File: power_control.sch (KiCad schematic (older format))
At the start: 64 parts, among them J26 Conn_01x02, J27 Conn_01x02, J28 Conn_01x02, J29 Conn_01x02, J30 Conn_01x02, J31 Conn_01x02, J32 Conn_01x02, J33 Conn_01x02, U10 DRV8801PWP, U11 DRV8801PWP, U12 DRV8801PWP, U5 DRV8801PWP, U6 DRV8801PWP, U7 DRV8801PWP, U8 DRV8801PWP, U9 DRV8801PWP

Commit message: Final touches
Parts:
- removed C13, C16, C22, C25, C28, C34: 100nF, lsts-passives:C_0603, symbol Device:C
- removed C21, C33: 100uF, Capacitor_THT:CP_Radial_D5.0mm_P2.00mm, symbol Device:CP
- removed J28, J31: Conn_01x02, Connector_Molex:Molex_Micro-Fit_3.0_43045-0212_2x01_P3.00mm_Vertical, symbol Connector_Generic:Conn_01x02
- removed R34, R35, R40, R41: 10kR, lsts-passives:R_0603, symbol Device:R
- removed U10, U7: DRV8801PWP, Package_SO:HTSSOP-16-1EP_4.4x5mm_P0.65mm_EP3.4x5mm_Mask3x3mm_ThermalVias, symbol Driver_Motor:DRV8801PWP
- C10: renamed from C19; symbol Device:CP -> power_board-rescue:CP-Device
- C11: renamed from C20; footprint lsts-passives:C_0603 -> lsts_passives:C_0603
- C12: renamed from C23; footprint lsts-passives:C_0603 -> lsts_passives:C_0603
- C13: renamed from C24; footprint lsts-passives:C_0603 -> lsts_passives:C_0603
- C14: renamed from C26; footprint lsts-passives:C_0603 -> lsts_passives:C_0603
- C15: renamed from C27; footprint lsts-passives:C_0603 -> lsts_passives:C_0603
- C16: renamed from C29; symbol Device:CP -> power_board-rescue:CP-Device
- C17: renamed from C30; footprint lsts-passives:C_0603 -> lsts_passives:C_0603
- C18: renamed from C31; symbol Device:CP -> power_board-rescue:CP-Device
- C19: renamed from C32; footprint lsts-passives:C_0603 -> lsts_passives:C_0603
- C20: renamed from C35; footprint lsts-passives:C_0603 -> lsts_passives:C_0603
- C21: renamed from C36; footprint lsts-passives:C_0603 -> lsts_passives:C_0603
- C22: renamed from C37; footprint lsts-passives:C_0603 -> lsts_passives:C_0603
- C23: renamed from C38; footprint lsts-passives:C_0603 -> lsts_passives:C_0603
- C24: renamed from C39; symbol Device:CP -> power_board-rescue:CP-Device
- C25: renamed from C40; footprint lsts-passives:C_0603 -> lsts_passives:C_0603
- C26: renamed from C41; symbol Device:CP -> power_board-rescue:CP-Device
- C27: renamed from C42; footprint lsts-passives:C_0603 -> lsts_passives:C_0603
- C4: renamed from C11; footprint lsts-passives:C_0603 -> lsts_passives:C_0603
- C5: renamed from C12; footprint lsts-passives:C_0603 -> lsts_passives:C_0603
- C6: renamed from C14; footprint lsts-passives:C_0603 -> lsts_passives:C_0603
- C7: renamed from C15; footprint lsts-passives:C_0603 -> lsts_passives:C_0603
- C8: renamed from C17; symbol Device:CP -> power_board-rescue:CP-Device
- C9: renamed from C18; footprint lsts-passives:C_0603 -> lsts_passives:C_0603
- R30, R31, R32, R33: footprint lsts-passives:R_0603 -> lsts_passives:R_0603
- R34: renamed from R36; footprint lsts-passives:R_0603 -> lsts_passives:R_0603
- R35: renamed from R37; footprint lsts-passives:R_0603 -> lsts_passives:R_0603
- R36: renamed from R38; footprint lsts-passives:R_0603 -> lsts_passives:R_0603
- R37: renamed from R39; footprint lsts-passives:R_0603 -> lsts_passives:R_0603
- R38: renamed from R42; footprint lsts-passives:R_0603 -> lsts_passives:R_0603
- R39: renamed from R43; footprint lsts-passives:R_0603 -> lsts_passives:R_0603
- R40: renamed from R44; footprint lsts-passives:R_0603 -> lsts_passives:R_0603
- R41: renamed from R45; footprint lsts-passives:R_0603 -> lsts_passives:R_0603
- renumbered J26 to J25, J27 to J26, J29 to J27, J30 to J28, J32 to J29, J33 to J30, U5 to U3, U6 to U4, U8 to U5, U9 to U6, U11 to U7, U12 to U8
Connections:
- net labels removed: MTR7_EN, MTR7_PH, MTR7_SL, MTR8_EN, MTR8_PH, MTR8_SL
- wire segments 224 -> 168
- no-connect marks 16 -> 12

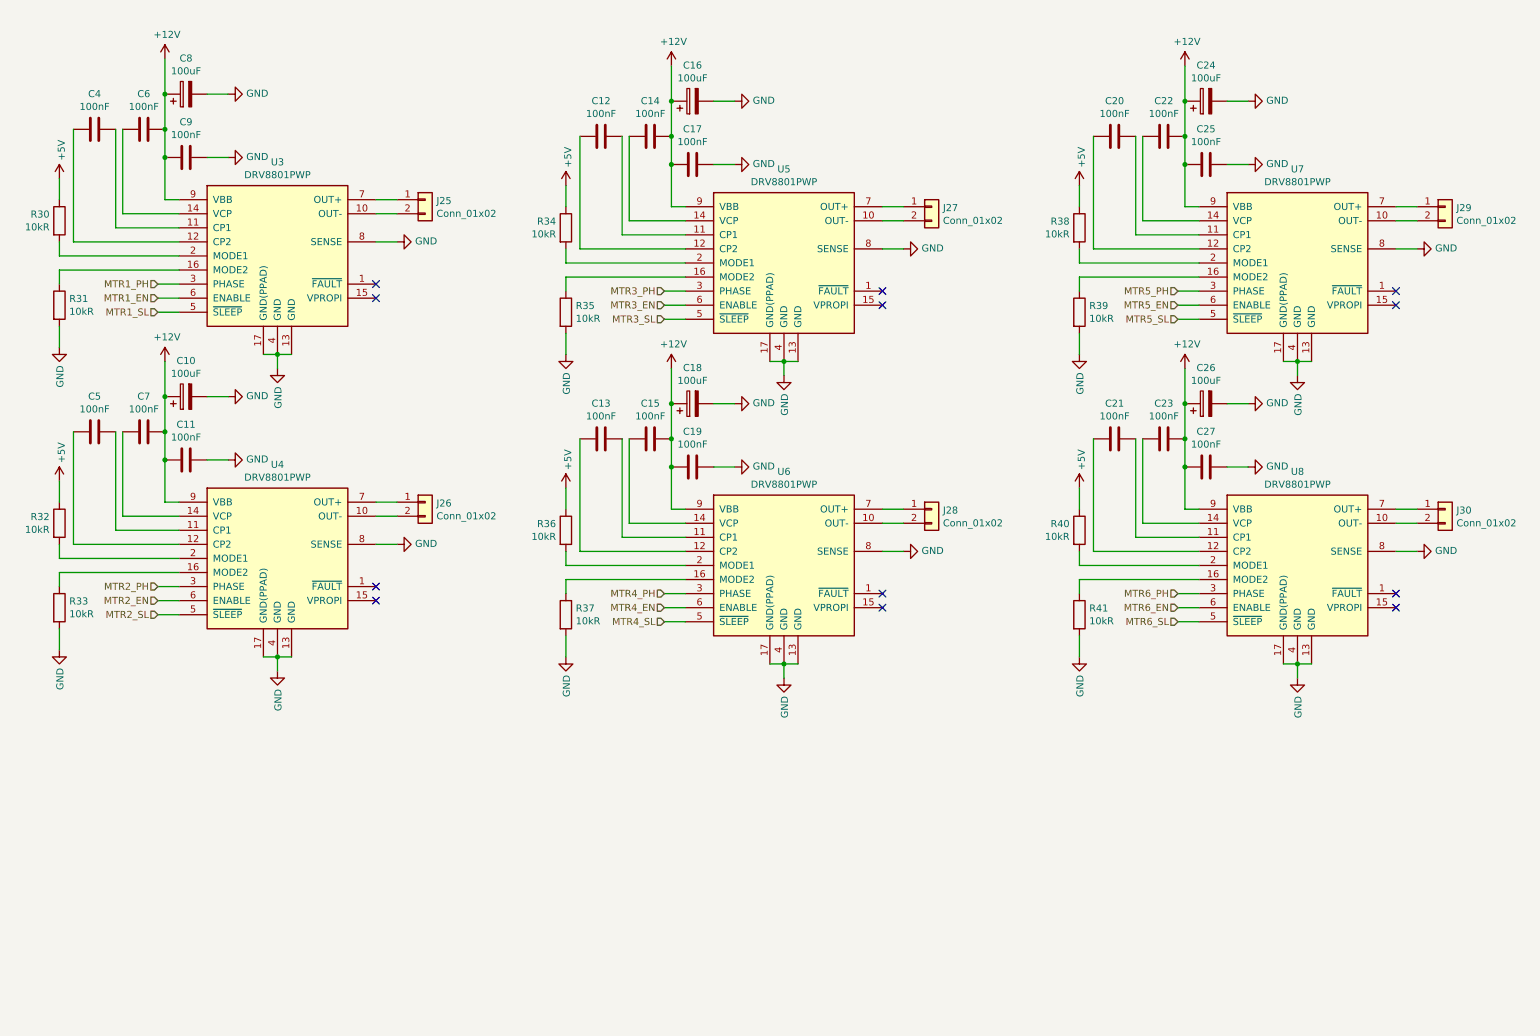
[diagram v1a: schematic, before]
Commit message: Replaced motor drivers
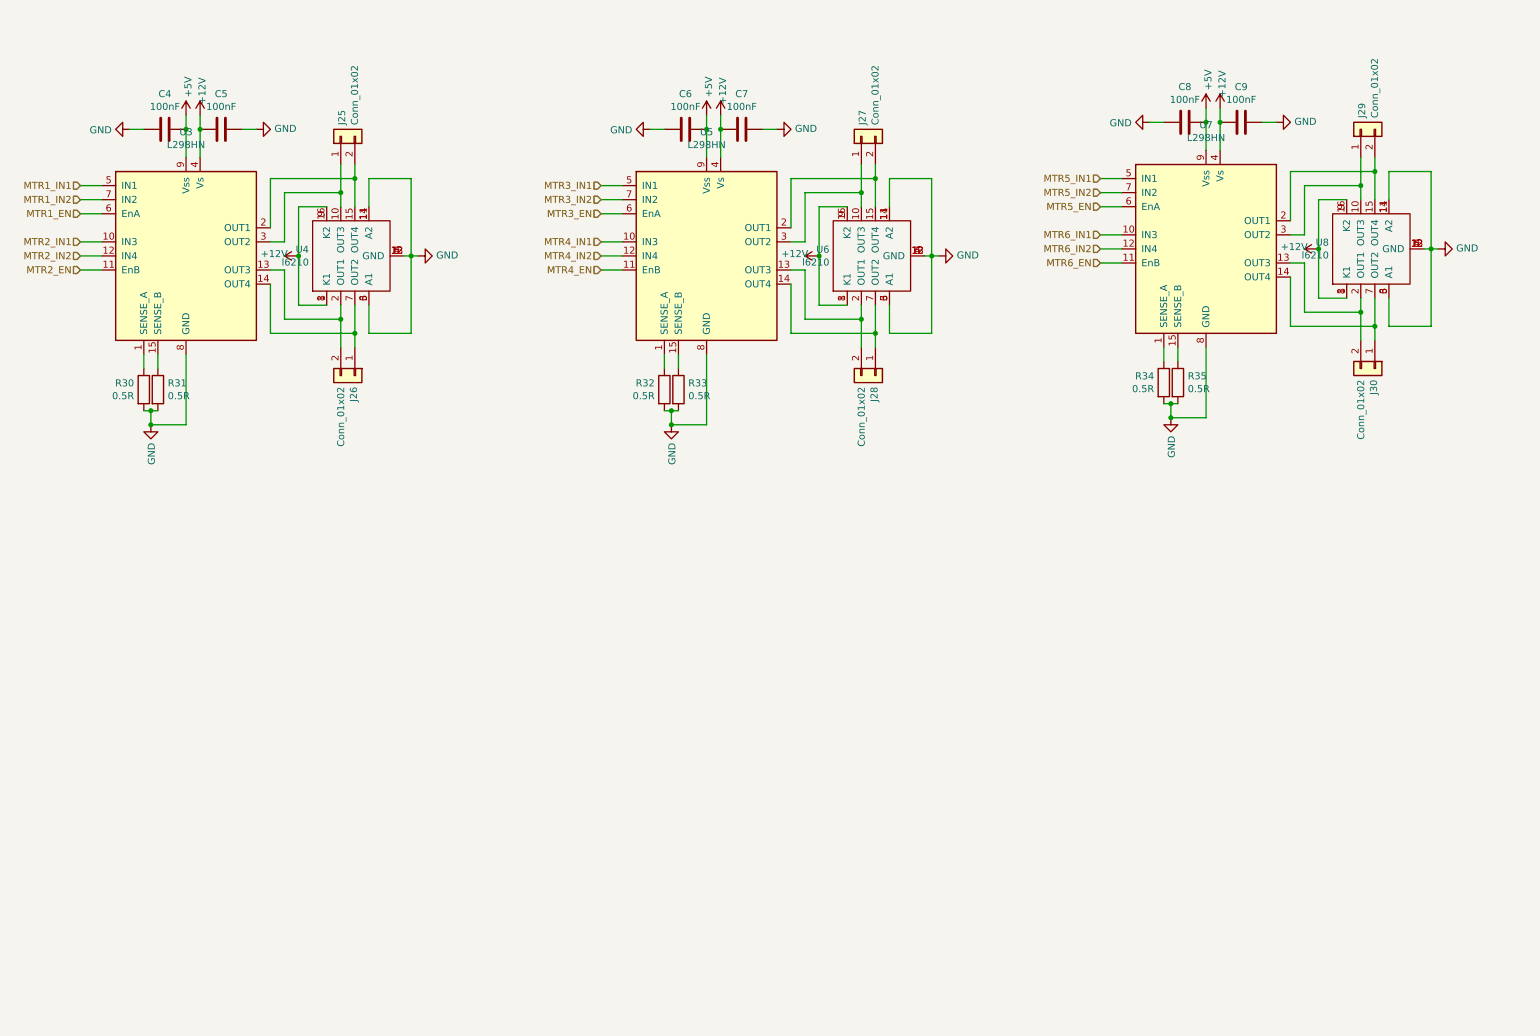
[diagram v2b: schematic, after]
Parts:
- removed C10, C16, C18, C24, C26, C8: 100uF, Capacitor_THT:CP_Radial_D5.0mm_P2.00mm, symbol power_board-rescue:CP-Device
- removed C11, C12, C13, C14, C15, C17, C19, C20, C21, C22, C23, C25, C27, C5: 100nF, lsts_passives:C_0603, symbol Device:C
- removed R30, R36, R37, R38, R39, R40, R41: 10kR, lsts_passives:R_0603, symbol Device:R
- removed U3, U4, U5, U6, U7, U8: DRV8801PWP, Package_SO:HTSSOP-16-1EP_4.4x5mm_P0.65mm_EP3.4x5mm_Mask3x3mm_ThermalVias, symbol Driver_Motor:DRV8801PWP
- added C6, C8: 100nF, lsts_passives:C_0603, symbol Device:C
- added R31: 0.5R, lsts_passives:R_0603, symbol Device:R
- added U3, U5, U7: L298HN, Package_TO_SOT_THT:TO-220-15_P2.54x2.54mm_StaggerOdd_Lead4.58mm_Vertical, symbol Driver_Motor:L298HN
- added U4, U6, U8: l6210, Package_DIP:DIP-16_W7.62mm, symbol Diode_Bridge:l6210
- R30: renamed from R31; value 10kR -> 0.5R
- R32, R33, R34, R35: value 10kR -> 0.5R
- renumbered C6 to C5
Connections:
- net +12V: now also C5.2, C7.2, U3.4 (Vs), U4.1 (K1), U4.16 (K2), U4.8 (K1), U4.9 (K2), U5.4 (Vs), U6.1 (K1), U6.16 (K2), U6.8 (K1), U6.9 (K2), U7.4 (Vs), U8.1 (K1), U8.16 (K2), U8.8 (K1), U8.9 (K2); no longer C5.1, C7.1
- net +5V: now also C4.1, C6.1, C8.1, U3.9 (Vss), U5.9 (Vss), U7.9 (Vss); no longer R32.1, R34.1
- net GND: now also C4.2, C5.1, C7.1, R32.2, R34.2, C6.2, C8.2, R31.2, U3.8 (GND), U4.11 (A2), U4.12 (GND), U4.13 (GND), U4.14 (A2), U4.3 (A1), U4.4 (GND), U4.5 (GND), U4.6 (A1), U5.8 (GND), U6.11 (A2), U6.12 (GND), U6.13 (GND), U6.14 (A2), U6.3 (A1), U6.4 (GND), U6.5 (GND), U6.6 (A1), U7.8 (GND), U8.11 (A2), U8.12 (GND), U8.13 (GND), U8.14 (A2), U8.3 (A1), U8.4 (GND), U8.5 (GND), U8.6 (A1)
- net MTR1_EN: now also U3.6 (EnA)
- net MTR2_EN: now also U3.11 (EnB)
- net MTR3_EN: now also U5.6 (EnA)
- net MTR4_EN: now also U5.11 (EnB)
- net MTR5_EN: now also U7.6 (EnA)
- net MTR6_EN: now also U7.11 (EnB)
- net at J25.1 (Pin_1): now also U3.3 (OUT2), U4.10 (OUT3)
- net at J25.2 (Pin_2): now also U3.2 (OUT1), U4.15 (OUT4)
- net at R30.1: now also U3.1 (SENSE_A)
- net at J26.2 (Pin_2): now also U3.13 (OUT3), U4.2 (OUT1)
- net at R33.1: now also U5.15 (SENSE_B)
- net at J26.1 (Pin_1): now also U3.14 (OUT4), U4.7 (OUT2)
- net at J27.2 (Pin_2): now also U5.2 (OUT1), U6.15 (OUT4)
- net at R35.1: now also U7.15 (SENSE_B)
- net at J27.1 (Pin_1): now also U5.3 (OUT2), U6.10 (OUT3)
- net at J28.2 (Pin_2): now also U5.13 (OUT3), U6.2 (OUT1)
- net at J28.1 (Pin_1): now also U5.14 (OUT4), U6.7 (OUT2)
- net at J29.2 (Pin_2): now also U7.2 (OUT1), U8.15 (OUT4)
- net at J29.1 (Pin_1): now also U7.3 (OUT2), U8.10 (OUT3)
- net at J30.2 (Pin_2): now also U7.13 (OUT3), U8.2 (OUT1)
- net at J30.1 (Pin_1): now also U7.14 (OUT4), U8.7 (OUT2)
- new net: R31.1, U3.15 (SENSE_B)
- new net: R32.1, U5.1 (SENSE_A)
- new net: R34.1, U7.1 (SENSE_A)
- new net MTR1_IN1: U3.5 (IN1)
- new net MTR1_IN2: U3.7 (IN2)
- new net MTR2_IN1: U3.10 (IN3)
- new net MTR2_IN2: U3.12 (IN4)
- new net MTR3_IN1: U5.5 (IN1)
- new net MTR3_IN2: U5.7 (IN2)
- new net MTR4_IN1: U5.10 (IN3)
- new net MTR4_IN2: U5.12 (IN4)
- new net MTR5_IN1: U7.5 (IN1)
- new net MTR5_IN2: U7.7 (IN2)
- new net MTR6_IN1: U7.10 (IN3)
- new net MTR6_IN2: U7.12 (IN4)
- no-connect marks 12 -> 0
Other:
- moved on the sheet: C4, C5, J25, J26, J27, J28, J29, J30, R30

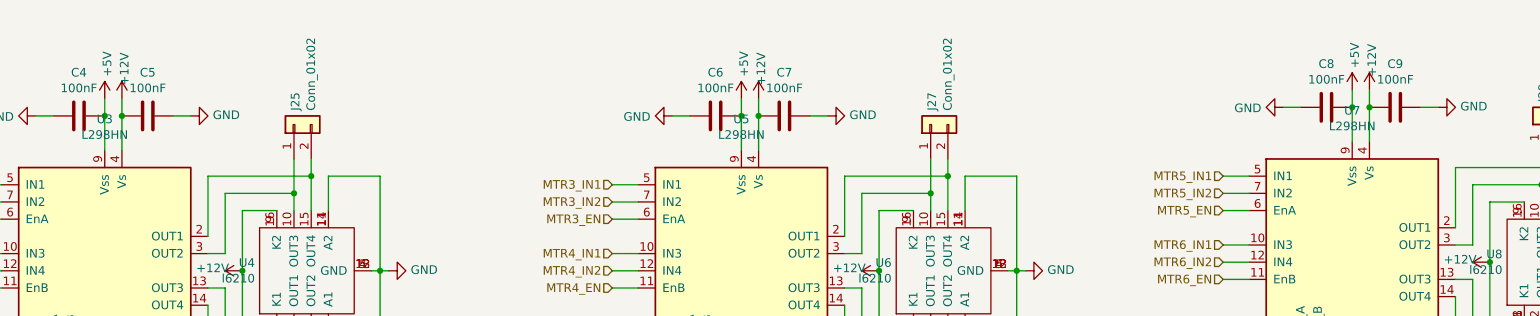
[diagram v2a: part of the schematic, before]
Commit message: Added 220uf capacitors
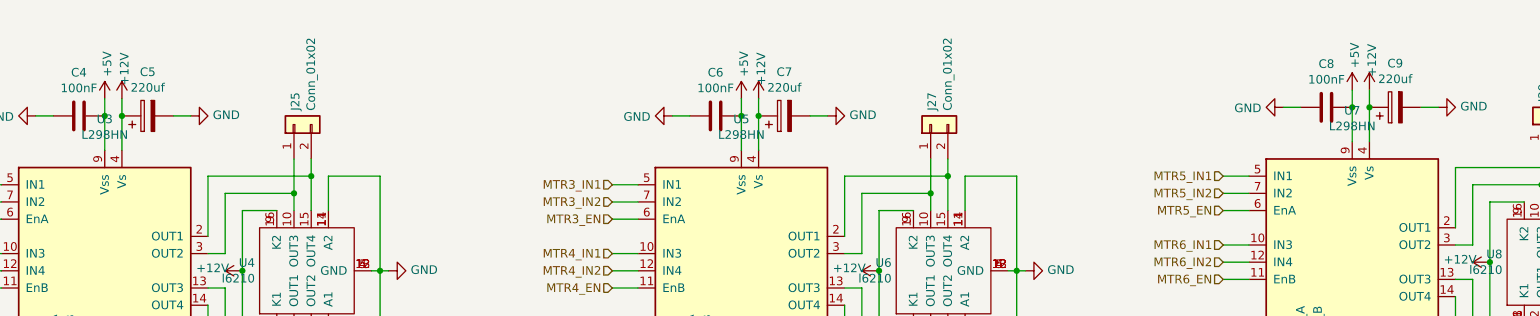
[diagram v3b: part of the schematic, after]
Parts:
- removed C5, C7, C9: 100nF, lsts_passives:C_0603, symbol Device:C
- added C5, C7, C9: 220uf, Capacitor_THT:CP_Radial_D10.0mm_P5.00mm, symbol Device:C_Polarized
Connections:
- net +12V: now also C5.1, C7.1, C9.1
- net GND: now also C5.2, C7.2, C9.2
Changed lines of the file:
@@
 	1    0    0    -1
-$EndComp
-$Comp
-L Device:C C5
-U 1 1 5E5F9468
-P 2000 1350
-F 0 "C5" V 1748 1350 50  0000 C CNN
-F 1 "100nF" V 1839 1350 50  0000 C CNN
-F 2 "lsts_passives:C_0603" H 2038 1200 50  0001 C CNN
-F 3 "~" H 2000 1350 50  0001 C CNN
-F 4 "EMK107B7104KAHT" H 2000 1350 50  0001 C CNN "manf#"
-	1    2000 1350
-	0    1    1    0
 $EndComp
 Text HLabel 1000 1750 0    50   Input ~ 0
@@
 	1450 1350 1350 1350
 Wire Wire Line
-	1850 1550 1850 1350
-Connection ~ 1850 1350
-Wire Wire Line
-	1850 1350 1850 1250
-Wire Wire Line
 	2250 1350 2150 1350
 Wire Wire Line
@@
 $EndComp
 $Comp
-L Device:C C7
-U 1 1 61999836
-P 5700 1350
-F 0 "C7" V 5448 1350 50  0000 C CNN
-F 1 "100nF" V 5539 1350 50  0000 C CNN
-F 2 "lsts_passives:C_0603" H 5738 1200 50  0001 C CNN
-F 3 "~" H 5700 1350 50  0001 C CNN
-F 4 "EMK107B7104KAHT" H 5700 1350 50  0001 C CNN "manf#"
-	1    5700 1350
-	0    1    1    0
-$EndComp
-$Comp
 L power:GND #PWR068
 U 1 1 6199983C
@@
 Wire Wire Line
 	5150 1350 5050 1350
-Wire Wire Line
-	5550 1550 5550 1350
-Connection ~ 5550 1350
-Wire Wire Line
-	5550 1350 5550 1250
 Wire Wire Line
 	5950 1350 5850 1350
@@
 $EndComp
 $Comp
-L Device:C C9
-U 1 1 619DDDA0
-P 9250 1300
-F 0 "C9" V 8998 1300 50  0000 C CNN
-F 1 "100nF" V 9089 1300 50  0000 C CNN
-F 2 "lsts_passives:C_0603" H 9288 1150 50  0001 C CNN
-F 3 "~" H 9250 1300 50  0001 C CNN
-F 4 "EMK107B7104KAHT" H 9250 1300 50  0001 C CNN "manf#"
-	1    9250 1300
-	0    1    1    0
-$EndComp
-$Comp
 L power:GND #PWR075
 U 1 1 619DDDA6
@@
 Wire Wire Line
 	8700 1300 8600 1300
-Wire Wire Line
-	9100 1500 9100 1300
-Connection ~ 9100 1300
-Wire Wire Line
-	9100 1300 9100 1200
 Wire Wire Line
 	9500 1300 9400 1300
@@
 Wire Wire Line
 	9600 2750 9600 2400
+$Comp
+L Device:C_Polarized C5
+U 1 1 61D58D79
+P 2000 1350
+F 0 "C5" V 2255 1350 50  0000 C CNN
+F 1 "220uf" V 2164 1350 50  0000 C CNN
+F 2 "Capacitor_THT:CP_Radial_D10.0mm_P5.00mm" H 2038 1200 50  0001 C CNN
+F 3 "MAL213668221E3" H 2000 1350 50  0001 C CNN
+	1    2000 1350
+	0    -1   -1   0
+$EndComp
+Wire Wire Line
+	1850 1250 1850 1350
+Connection ~ 1850 1350
+Wire Wire Line
+	1850 1350 1850 1550
+Wire Wire Line
+	5550 1250 5550 1350
+Wire Wire Line
+	9100 1200 9100 1300
+$Comp
+L Device:C_Polarized C7
+U 1 1 61D685B1
+P 5700 1350
+F 0 "C7" V 5955 1350 50  0000 C CNN
+F 1 "220uf" V 5864 1350 50  0000 C CNN
+F 2 "Capacitor_THT:CP_Radial_D10.0mm_P5.00mm" H 5738 1200 50  0001 C CNN
+F 3 "MAL213668221E3" H 5700 1350 50  0001 C CNN
+	1    5700 1350
+	0    -1   -1   0
+$EndComp
+Connection ~ 5550 1350
+Wire Wire Line
+	5550 1350 5550 1550
+$Comp
+L Device:C_Polarized C9
+U 1 1 61D68D92
+P 9250 1300
+F 0 "C9" V 9505 1300 50  0000 C CNN
+F 1 "220uf" V 9414 1300 50  0000 C CNN
+F 2 "Capacitor_THT:CP_Radial_D10.0mm_P5.00mm" H 9288 1150 50  0001 C CNN
+F 3 "MAL213668221E3" H 9250 1300 50  0001 C CNN
+	1    9250 1300
+	0    -1   -1   0
+$EndComp
+Connection ~ 9100 1300
+Wire Wire Line
+	9100 1300 9100 1500
 $EndSCHEMATC

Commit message: Changed sense resistor footprint
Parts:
- R30, R31, R32, R33, R34, R35: footprint lsts_passives:R_0603 -> lsts_passives:R_0805
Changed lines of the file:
@@
 F 0 "R30" H 1381 3246 50  0000 R CNN
 F 1 "0.5R" H 1381 3155 50  0000 R CNN
-F 2 "lsts_passives:R_0603" V 1380 3200 50  0001 C CNN
+F 2 "lsts_passives:R_0805" V 1380 3200 50  0001 C CNN
 F 3 "~" H 1450 3200 50  0001 C CNN
 F 4 "CRCW060310K0JNEBC" H 1450 3200 50  0001 C CNN "manf#"
@@
 F 0 "R31" H 1620 3246 50  0000 L CNN
 F 1 "0.5R" H 1620 3155 50  0000 L CNN
-F 2 "lsts_passives:R_0603" V 1480 3200 50  0001 C CNN
+F 2 "lsts_passives:R_0805" V 1480 3200 50  0001 C CNN
 F 3 "~" H 1550 3200 50  0001 C CNN
 F 4 "CRCW060310K0JNEBC" H 1550 3200 50  0001 C CNN "manf#"
@@
 F 0 "R32" H 5081 3246 50  0000 R CNN
 F 1 "0.5R" H 5081 3155 50  0000 R CNN
-F 2 "lsts_passives:R_0603" V 5080 3200 50  0001 C CNN
+F 2 "lsts_passives:R_0805" V 5080 3200 50  0001 C CNN
 F 3 "~" H 5150 3200 50  0001 C CNN
 F 4 "CRCW060310K0JNEBC" H 5150 3200 50  0001 C CNN "manf#"
@@
 F 0 "R33" H 5320 3246 50  0000 L CNN
 F 1 "0.5R" H 5320 3155 50  0000 L CNN
-F 2 "lsts_passives:R_0603" V 5180 3200 50  0001 C CNN
+F 2 "lsts_passives:R_0805" V 5180 3200 50  0001 C CNN
 F 3 "~" H 5250 3200 50  0001 C CNN
 F 4 "CRCW060310K0JNEBC" H 5250 3200 50  0001 C CNN "manf#"
@@
 F 0 "R34" H 8631 3196 50  0000 R CNN
 F 1 "0.5R" H 8631 3105 50  0000 R CNN
-F 2 "lsts_passives:R_0603" V 8630 3150 50  0001 C CNN
+F 2 "lsts_passives:R_0805" V 8630 3150 50  0001 C CNN
 F 3 "~" H 8700 3150 50  0001 C CNN
 F 4 "CRCW060310K0JNEBC" H 8700 3150 50  0001 C CNN "manf#"
@@
 F 0 "R35" H 8870 3196 50  0000 L CNN
 F 1 "0.5R" H 8870 3105 50  0000 L CNN
-F 2 "lsts_passives:R_0603" V 8730 3150 50  0001 C CNN
+F 2 "lsts_passives:R_0805" V 8730 3150 50  0001 C CNN
 F 3 "~" H 8800 3150 50  0001 C CNN
 F 4 "CRCW060310K0JNEBC" H 8800 3150 50  0001 C CNN "manf#"
